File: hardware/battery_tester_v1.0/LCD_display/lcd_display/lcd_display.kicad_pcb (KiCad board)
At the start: 2 copper layers, 99.5 x 99.5 mm, 63 parts, among them J1 VCC_5V, J2 LED, J3 LED, Q1 BC817, SW1 SW_Push, SW2 SW_Push, SW3 SW_Push, SW4 SW_Push, SW5 SW_Push, SW6 SW_Push, SW7 SW_Push, SW8 SW_Push, SW9 SW_Push, U1 74AHCT244, U2 74HCT125, U3 74HC595, U4 74HC595

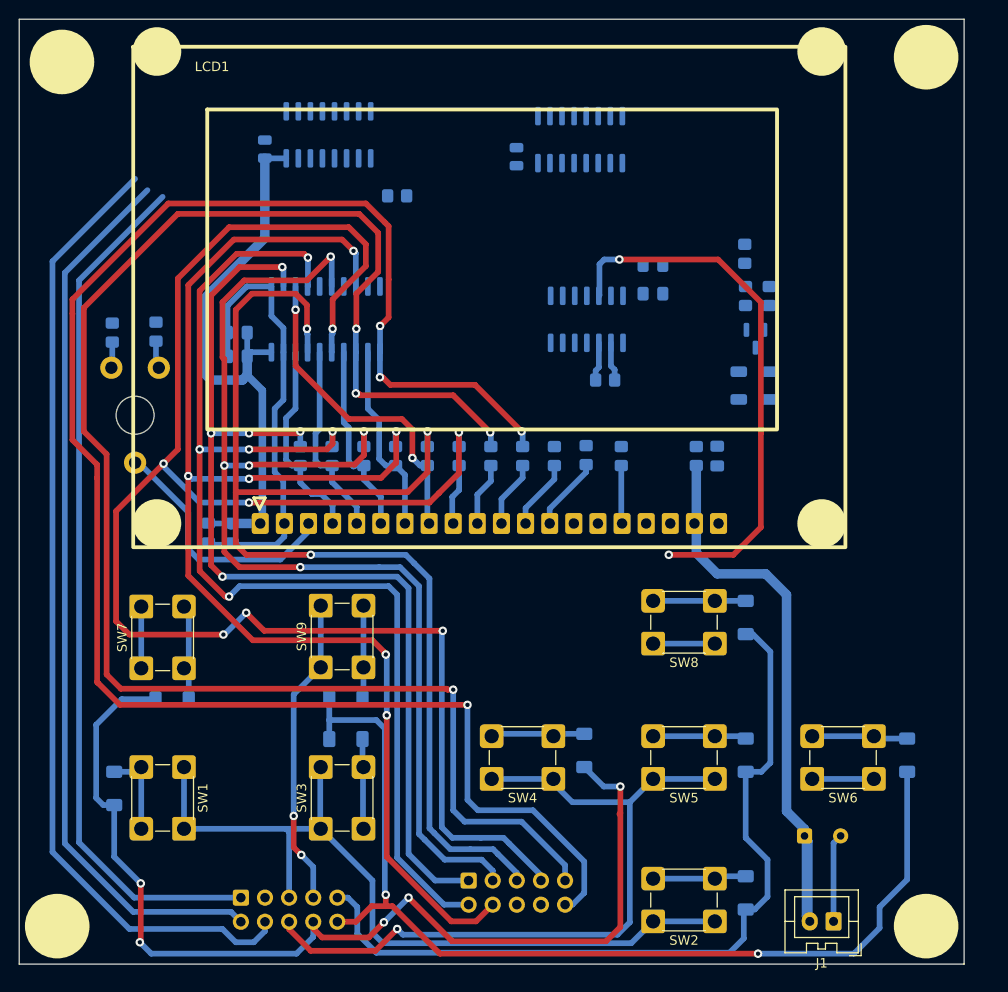
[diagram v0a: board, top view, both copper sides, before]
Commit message: update lcd display + button pcb
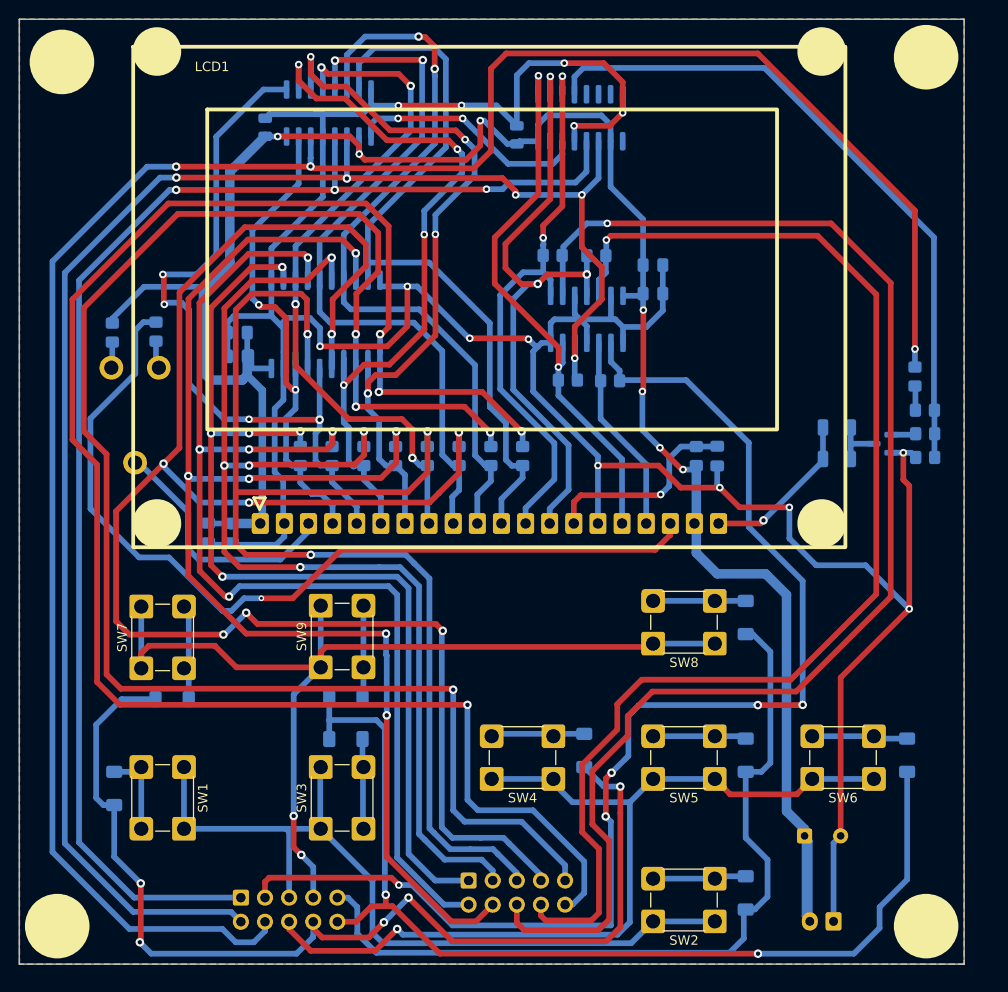
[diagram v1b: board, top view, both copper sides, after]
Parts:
- J1: moved to B.Cu
- U1: footprint Package_SO:SO-20_5.3x12.6mm_P1.27mm -> Package_SO:SOIC-20W_7.5x12.8mm_P1.27mm
- moved R21 57.8 mm to (186.3, 66.6), turned to 90 degrees
- moved R15 25.1 mm to (187.4, 70.2), turned to 180 degrees
- moved R17 23.8 mm to (187.4, 72.7), turned to 180 degrees
- moved R16 23.6 mm to (187.4, 75.2), turned to 0 degrees
- moved R11 21.1 mm to (148.2, 53.9), turned to 0 degrees
- moved R12 21.0 mm to (152.8, 53.9), turned to 0 degrees
- moved Q1 17.3 mm to (182.9, 73.7), turned to 180 degrees
- moved R18 12.9 mm to (178.1, 75.3), turned to 0 degrees
- moved R13 9.78 mm to (149.8, 67.0), turned to 0 degrees
- moved R20 8.29 mm to (178.1, 72.0), turned to 0 degrees
- moved C10 2.30 mm to (144.4, 41.2)
- moved C9 2.30 mm to (117.9, 40.4)
- moved U3 2.30 mm to (124.6, 38.9)
- moved U4 2.30 mm to (151.1, 39.4)
- moved R14 0.53 mm to (154.2, 67.1)
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- renumbered C9 to C10, C10 to C3, C3 to C4, C4 to C5, C5 to C6, C6 to C7, C7 to C8, C8 to C9, R14 to R13, R15 to R14, R16 to R15, R17 to R16, R18 to R17, R19 to R18, R21 to R19, R13 to R21
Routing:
- net GND: track 56.2 -> 317.9 mm, vias 0 -> 14
- net CS1_IN: track 0.00 -> 145.4 mm, vias 0 -> 1
- net EN_IN: track 4.09 -> 133.2 mm, vias 0 -> 5
- net DATA: track 102.3 -> 221.6 mm, vias 0 -> 3
- net +5V: track 130.1 -> 235.7 mm, vias 0 -> 7
- net Net-(LCD1-VEE): track 0.00 -> 93.3 mm, vias 0 -> 1
- net CLK: track 94.4 -> 175.7 mm, vias 0 -> 5
- net CS2_IN: track 57.0 -> 133.1 mm, vias 2 -> 1
- net DB6: track 6.69 -> 79.9 mm, vias 0 -> 2
- net DB7: track 7.02 -> 80.0 mm
- net DB5: track 6.44 -> 77.6 mm, vias 0 -> 2
- net BACKLIGHT_DRIVE: track 0.00 -> 70.5 mm
- net CS2: track 7.79 -> 68.0 mm, vias 0 -> 3
- net COL3: track 45.8 -> 104.5 mm
- net DB3: track 20.3 -> 77.7 mm, vias 0 -> 4
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- added copper zone on B.Cu, net GND
- added copper zone on F.Cu, net GND

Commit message: lcd pcb done
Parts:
- added D10: LED, LED_THT:LED_D5.0mm, F.Cu at (184.2, 41.4)
- added D11: LED, LED_THT:LED_D5.0mm, F.Cu at (184.2, 50.4)
- added D12: LED, LED_THT:LED_D5.0mm, F.Cu at (184.2, 59.4)
- added Q2: BC817, Package_TO_SOT_SMD:SOT-23, B.Cu at (178.7, 38.5)
- added Q3: BC817, Package_TO_SOT_SMD:SOT-23, B.Cu at (179.6, 50.3)
- added Q4: BC817, Package_TO_SOT_SMD:SOT-23, B.Cu at (179.5, 58.9)
- added R22: 10k, Resistor_SMD:R_0805_2012Metric_Pad1.20x1.40mm_HandSolder, B.Cu at (176.2, 50.4)
- added R23: 10k, Resistor_SMD:R_0805_2012Metric_Pad1.20x1.40mm_HandSolder, B.Cu at (175.4, 38.7)
- added R24: 220R, Resistor_SMD:R_0805_2012Metric_Pad1.20x1.40mm_HandSolder, B.Cu at (182.7, 38.5)
- added R25: 220R, Resistor_SMD:R_0805_2012Metric_Pad1.20x1.40mm_HandSolder, B.Cu at (182.6, 47.9)
- added R26: 10k, Resistor_SMD:R_0805_2012Metric_Pad1.20x1.40mm_HandSolder, B.Cu at (177.8, 55.5)
- added R27: 220R, Resistor_SMD:R_0805_2012Metric_Pad1.20x1.40mm_HandSolder, B.Cu at (181.9, 62.2)
- R16: value 10k -> 100k
- moved R16 16.8 mm to (173.2, 66.3)
- moved R17 16.8 mm to (173.2, 63.8)
- moved Q1 16.8 mm to (168.7, 64.8)
- moved R15 16.8 mm to (173.2, 61.3)
- moved R21 16.8 mm to (172.1, 57.7)
- moved R20 7.39 mm to (170.7, 72.0), turned to 90 degrees
- moved R18 5.56 mm to (173.6, 72.0), turned to 90 degrees
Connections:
- U4 pad 5: unconnected-(U4-QF-Pad5) -> LED1
- U4 pad 6: unconnected-(U4-QG-Pad6) -> LED2
- U4 pad 7: unconnected-(U4-QH-Pad7) -> LED3
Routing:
- net +5V: track 235.7 -> 343.2 mm, vias 7 -> 10
- net GND: track 317.9 -> 403.7 mm, vias 14 -> 24
- net LED3: track 0.00 -> 39.5 mm
- net LED2: track 0.00 -> 35.3 mm
- net LED1: track 0.00 -> 29.3 mm
- net DATA: track 221.6 -> 202.2 mm
- net BACKLIGHT_DRIVE: track 70.5 -> 55.3 mm, vias 0 -> 2
- net CS1_IN: track 145.4 -> 135.1 mm
- net CS2_IN: track 133.1 -> 123.3 mm
- net Net-(Q1-C): track 5.74 -> 10.5 mm
- net Net-(D12-K): track 0.00 -> 3.38 mm
- net Net-(Q3-C): track 0.00 -> 3.17 mm
- net Net-(D10-K): track 0.00 -> 3.04 mm
- net Net-(Q4-C): track 0.00 -> 3.01 mm
- net Net-(D11-K): track 0.00 -> 2.80 mm
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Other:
- board text added: "+5V"
- board text added: "74AHCT244"
- board text added: "74HCT125"
- board text added: "74HCT595"
- board text added: "A"
- board text added: "CONTRAST"
- board text added: "CS1"
- board text added: "CS2"
- board text added: "DB0"
- board text added: "DB0 DB2 DB4 DB5 DB6"
- board text added: "DB1"
- board text added: "DB1 DB3 CS1 CS2 DB7"
- board text added: "DB2"
- board text added: "DB3"
- board text added: "DB4"
- board text added: "DB5"
- board text added: "DB6"
- board text added: "DI"
- board text added: "DOWN"
- board text added: "Display and button module kwiecinski.github.com 01.2026 V1.0"
- board text added: "EN"
- board text added: "F1"
- board text added: "F2"
- board text added: "F3"
- board text added: "F4"
- board text added: "GND"
- board text added: "K"
- board text added: "LAT EN COL1 COL3 ROW2 CLK DAT COL2 ROW1 ROW3"
- board text added: "LEFT"
- board text added: "M2,5"
- board text added: "OK"
- board text added: "RIGHT"
- board text added: "SB7"
- board text added: "UP"
- board text added: "VEE"
- board text added: "VO"
- board text added: "~{RST}"
